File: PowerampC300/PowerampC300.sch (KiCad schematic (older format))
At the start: 114 parts, among them J1 Conn_01x02, J2 Conn_01x02, J3 Conn_01x02, J4 Conn_01x01, J5 Conn_01x01, J6 Conn_01x01, J7 Conn_01x01, J8 Conn_01x02, J9 Conn_Coaxial, Q1 2N5551, Q10 MJE15033, Q11 MJE15032, Q12 MJE15032, Q13 2N5551, Q14 2N5401, Q15 MJE15032, Q16 MJE15033, Q17 MJL3281A, Q18 MJL1302A, Q19 MJL3281A, Q2 2N5551, Q20 MJL1302A, Q21 MJL3281A, Q22 MJL1302A, Q23 MJL3281A, Q24 MJL1302A, Q3 2N5401, Q4 2N5401, Q5 2N5551, Q6 2N5551, Q7 2N5551, Q8 2N5401

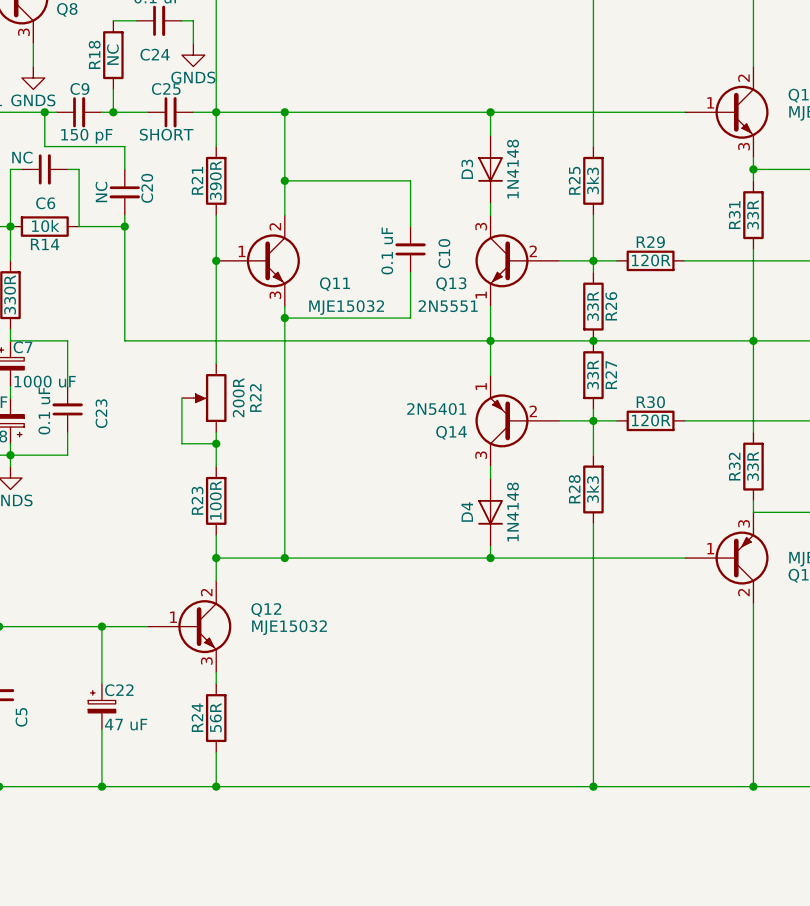
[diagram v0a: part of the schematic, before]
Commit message: Changed components for lower quiescent power
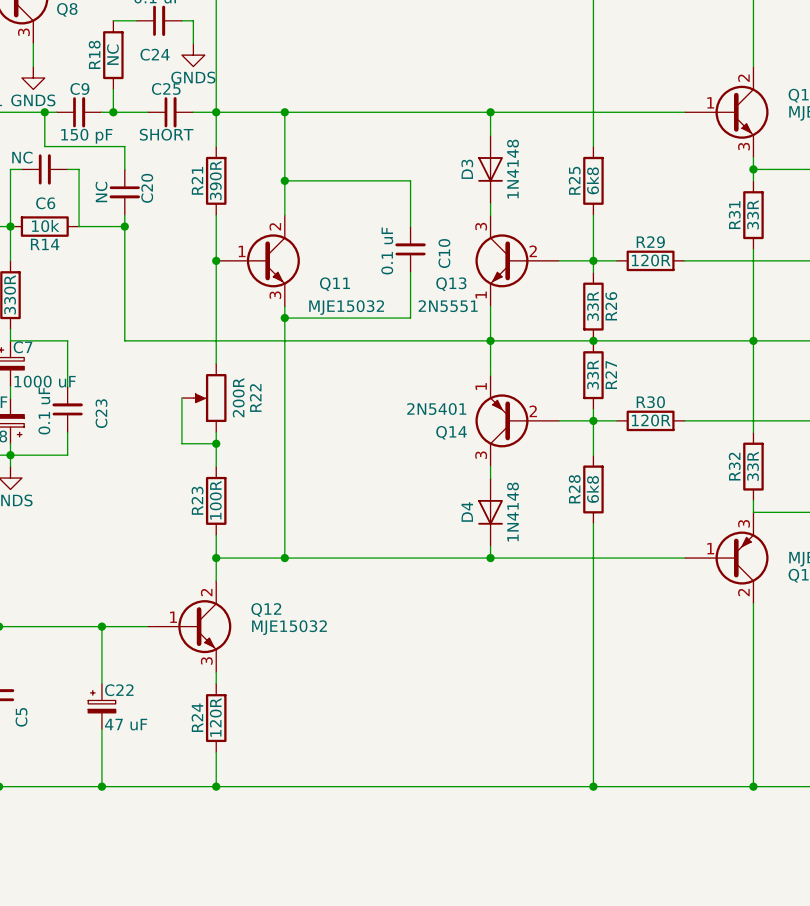
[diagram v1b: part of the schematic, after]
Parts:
- R24: value 56R -> 120R
- R25, R28: value 3k3 -> 6k8
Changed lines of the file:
@@
 P 3900 5850
 F 0 "R24" V 3980 5850 50  0000 C CNN
-F 1 "56R" V 3900 5850 50  0000 C CNN
+F 1 "120R" V 3900 5850 50  0000 C CNN
 F 2 "Resistors_THT:R_Axial_DIN0207_L6.3mm_D2.5mm_P7.62mm_Horizontal" V 3830 5850 50  0001 C CNN
 F 3 "" H 3900 5850 50  0001 C CNN
@@
 P 5550 3500
 F 0 "R25" V 5630 3500 50  0000 C CNN
-F 1 "3k3" V 5550 3500 50  0000 C CNN
+F 1 "6k8" V 5550 3500 50  0000 C CNN
 F 2 "Resistors_THT:R_Axial_DIN0411_L9.9mm_D3.6mm_P15.24mm_Horizontal" V 5480 3500 50  0001 C CNN
 F 3 "" H 5550 3500 50  0001 C CNN
@@
 P 5550 4850
 F 0 "R28" V 5630 4850 50  0000 C CNN
-F 1 "3k3" V 5550 4850 50  0000 C CNN
+F 1 "6k8" V 5550 4850 50  0000 C CNN
 F 2 "Resistors_THT:R_Axial_DIN0411_L9.9mm_D3.6mm_P15.24mm_Horizontal" V 5480 4850 50  0001 C CNN
 F 3 "" H 5550 4850 50  0001 C CNN

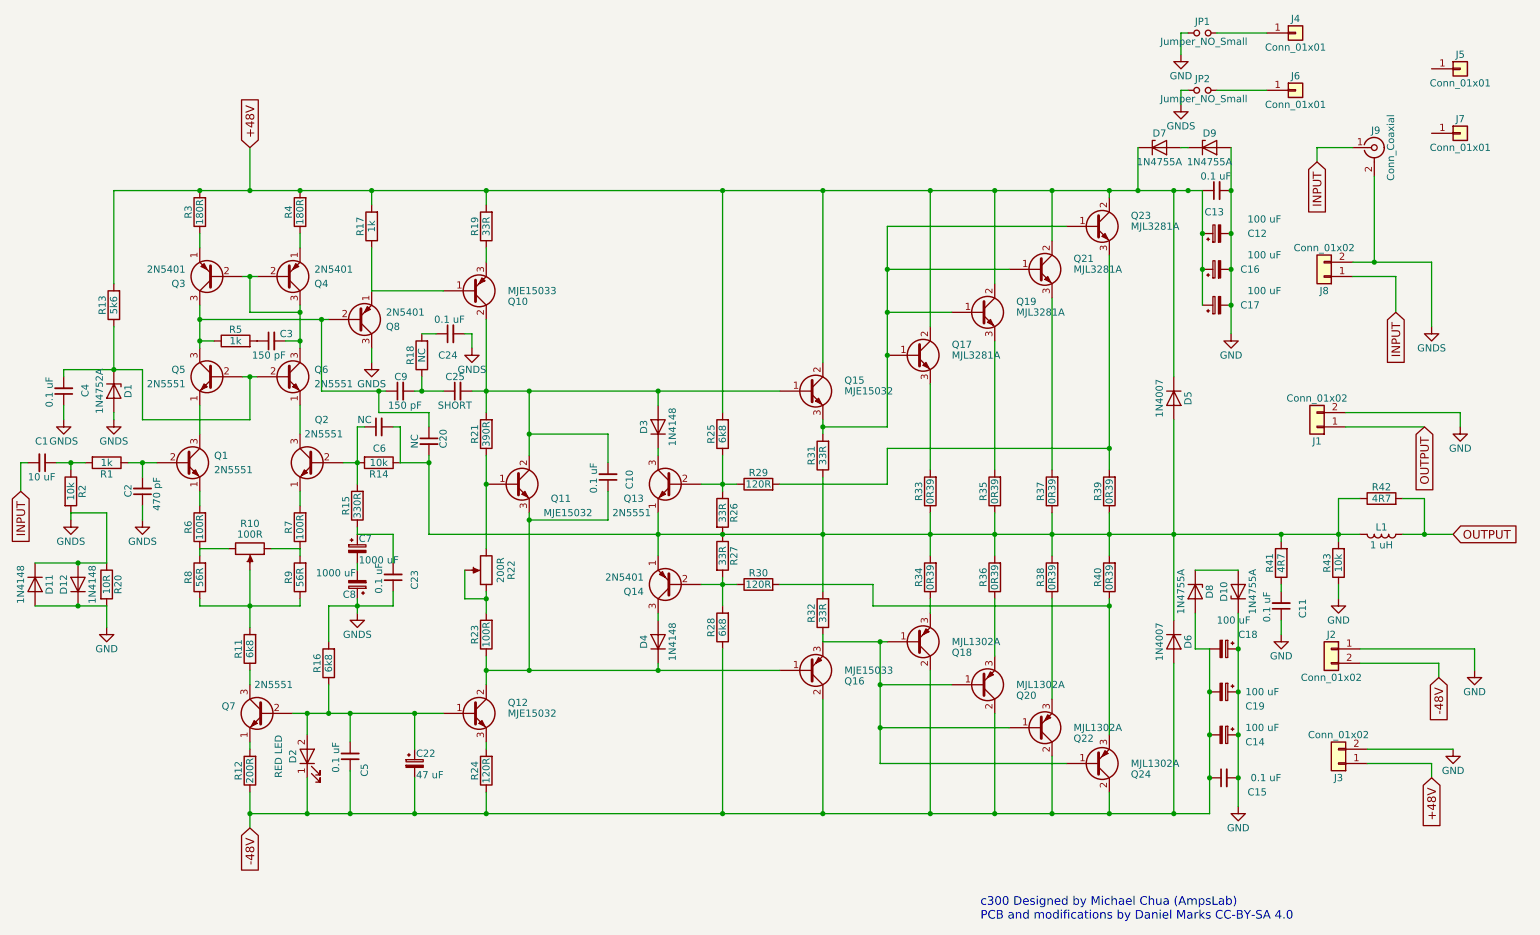
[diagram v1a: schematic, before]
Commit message: Added base stopper resistors
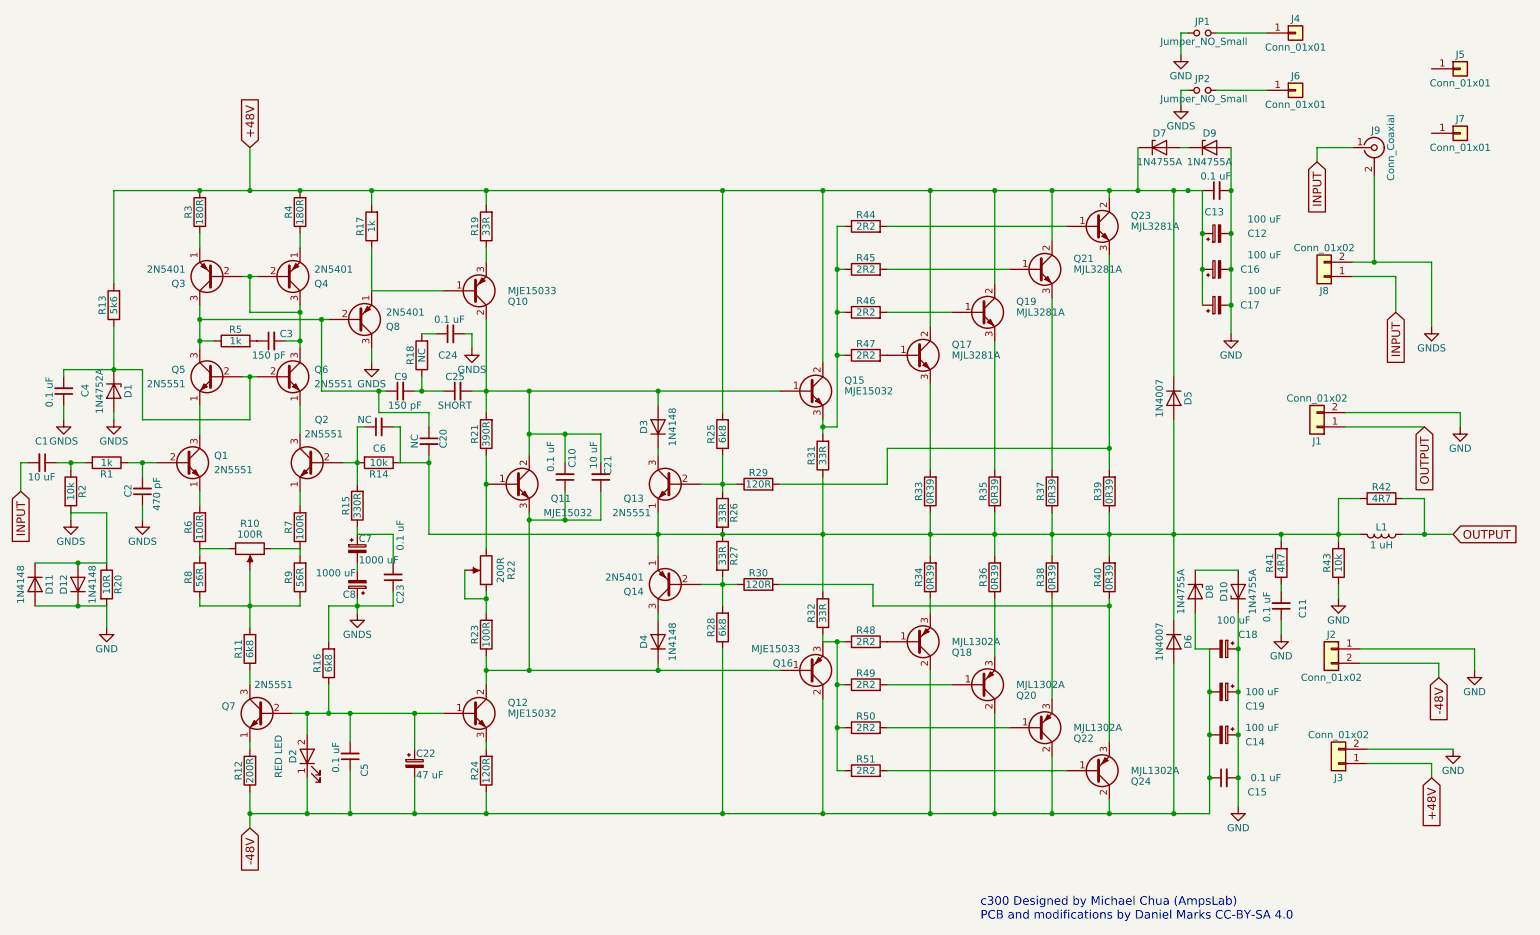
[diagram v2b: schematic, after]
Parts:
- added C21: 10 uF, Capacitors_THT:C_Disc_D5.0mm_W2.5mm_P5.00mm, symbol C_Small
- added R44, R45, R46, R47, R48, R49, R50, R51: 2R2, Resistors_THT:R_Axial_DIN0411_L9.9mm_D3.6mm_P15.24mm_Horizontal, symbol R
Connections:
- net at C10.1, D4.1 (K), Q11.3 (E)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: now also C21.1
- net at C10.2, C25.2, D3.2 (A)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: now also C21.2
- new net: Q15.3 (E), R31.2, R44.1, R45.1, R46.1, R47.1
- new net: Q16.3 (E), R32.1, R48.1, R49.1, R50.1, R51.1
- new net: Q17.1 (B), R47.2
- new net: Q18.1 (B), R48.2
- new net: Q19.1 (B), R46.2
- new net: Q21.1 (B), R45.2
- new net: Q23.1 (B), R44.2
- new net: Q20.1 (B), R49.2
- new net: Q22.1 (B), R50.2
- new net: Q24.1 (B), R51.2
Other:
- moved on the sheet: C10, Q24

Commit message: Additions of optional zener diodes to limit current surges
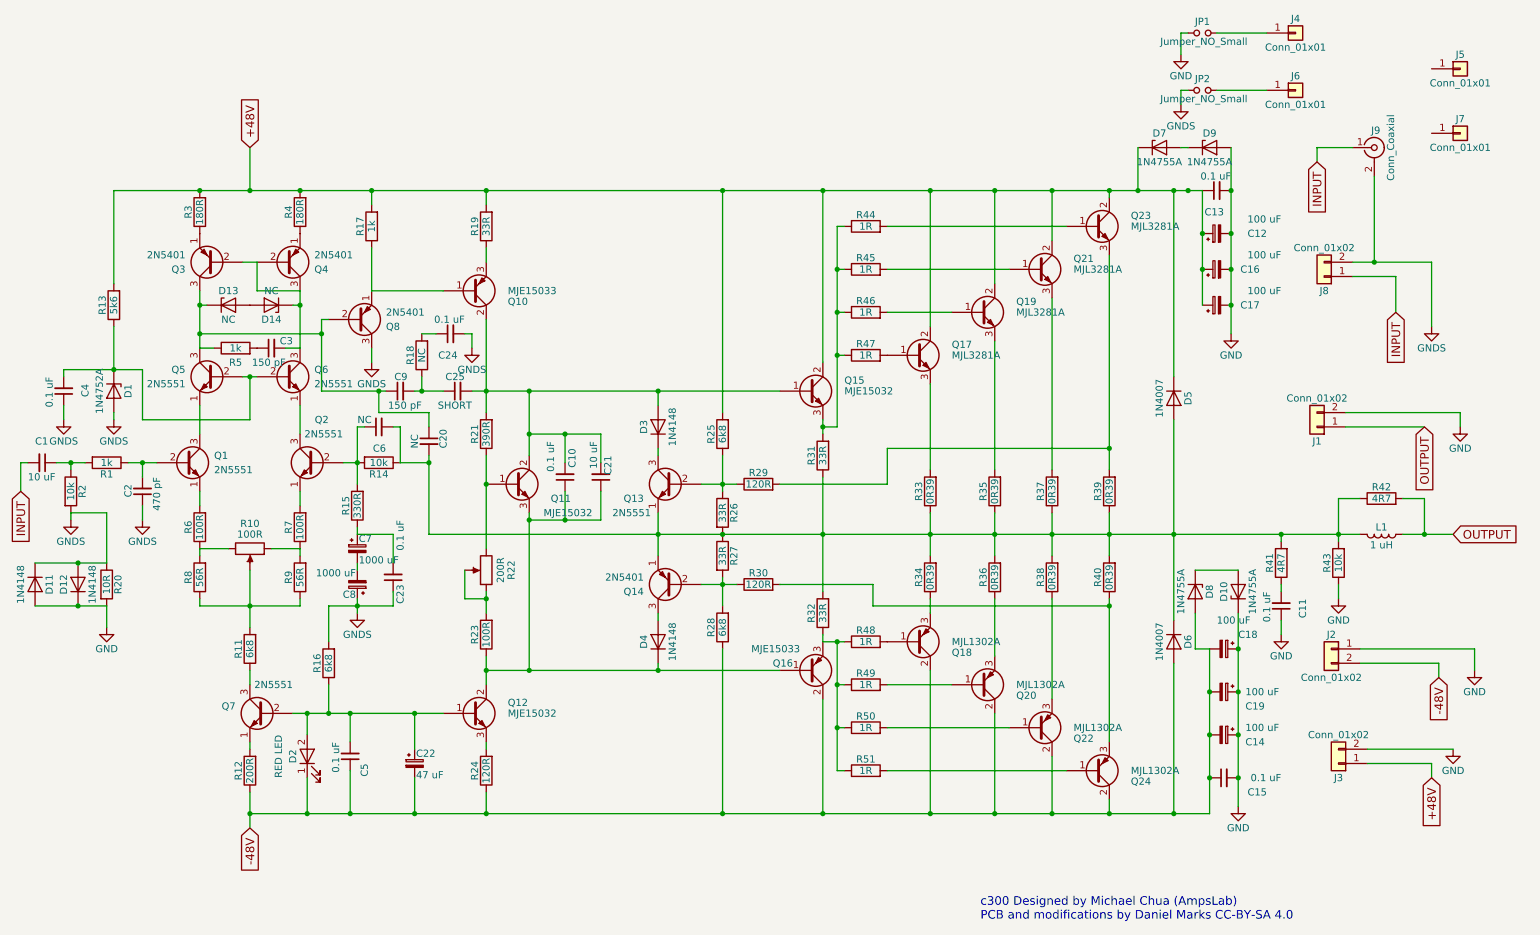
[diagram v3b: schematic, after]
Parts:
- added D13, D14: NC, Diodes_THT:D_DO-41_SOD81_P7.62mm_Horizontal, symbol D_Zener
- C2: footprint Capacitors_THT:C_Axial_L3.8mm_D2.6mm_P7.50mm_Horizontal -> Capacitors_THT:C_Rect_L7.0mm_W3.5mm_P5.00mm
- R44, R45, R46, R47, R48, R49, R50, R51: value 2R2 -> 1R
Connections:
- net at C20.1, C9.1, Q3.3 (C)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: now also D13.1 (K)
- net at C3.2, Q3.2 (B), Q4.2 (B)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: now also D14.1 (K)
- new net: D13.2 (A), D14.2 (A)
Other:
- moved on the sheet: C3, Q3, Q4, R5
